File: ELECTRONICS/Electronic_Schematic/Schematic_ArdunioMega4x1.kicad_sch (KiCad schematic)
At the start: 66 parts, among them J1 AudioJack2

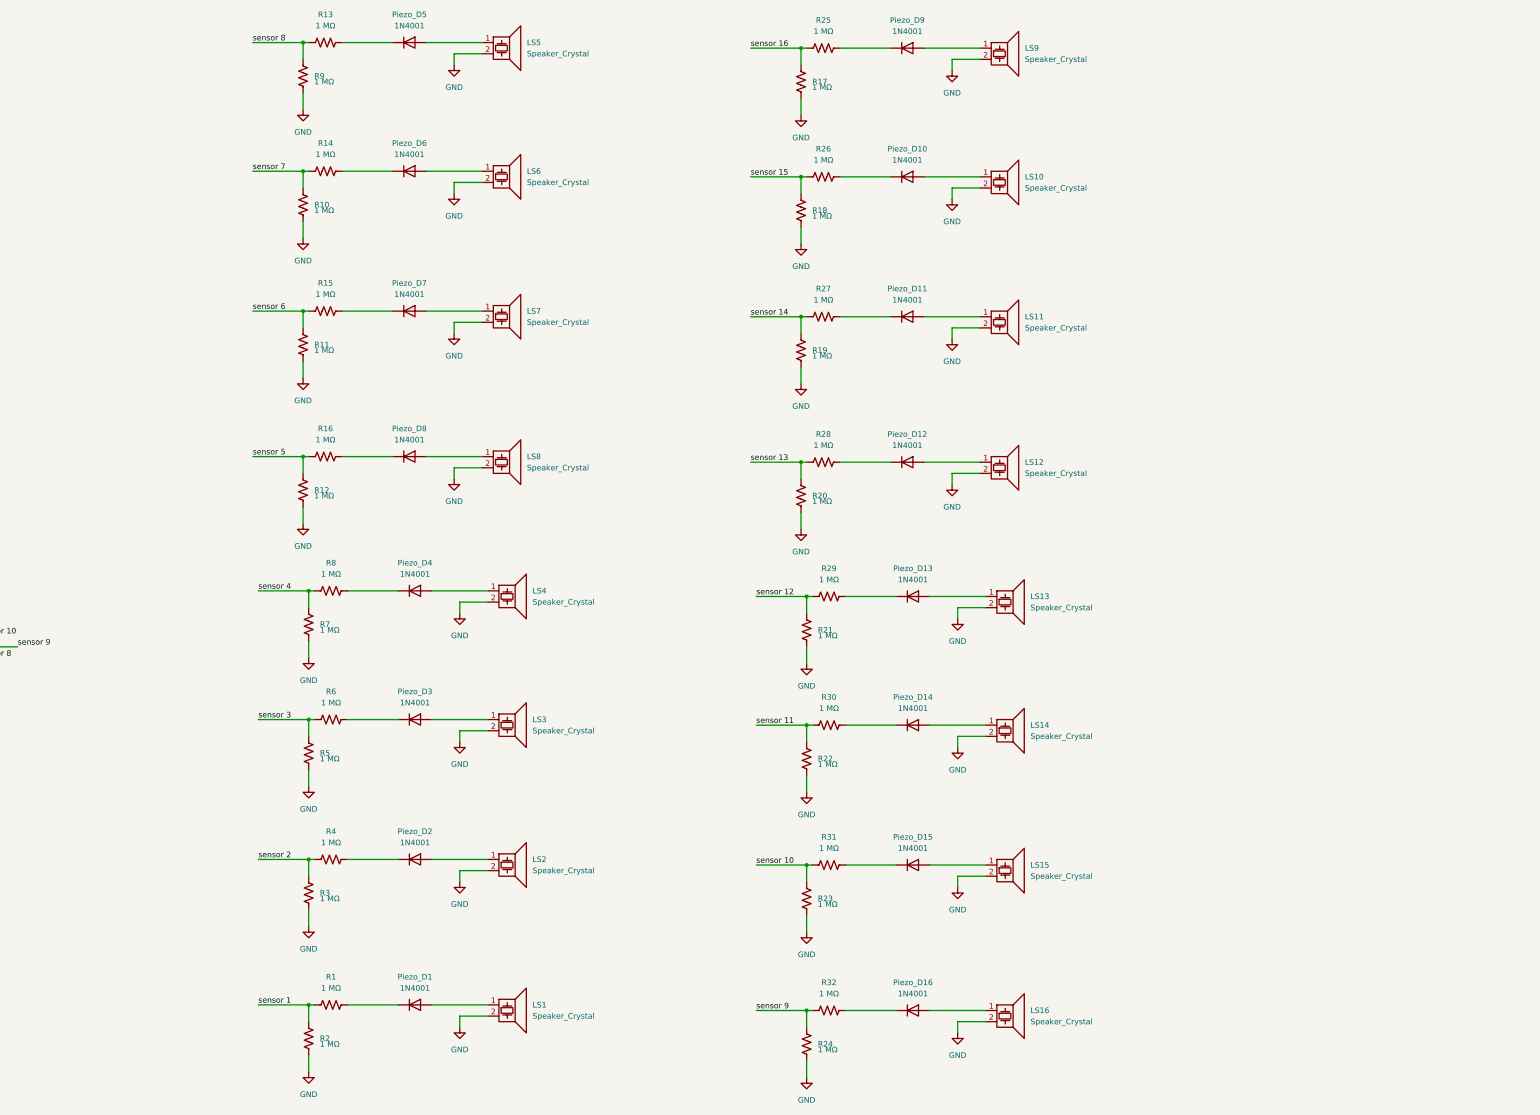
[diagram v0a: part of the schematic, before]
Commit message: added revision 3 of schematic
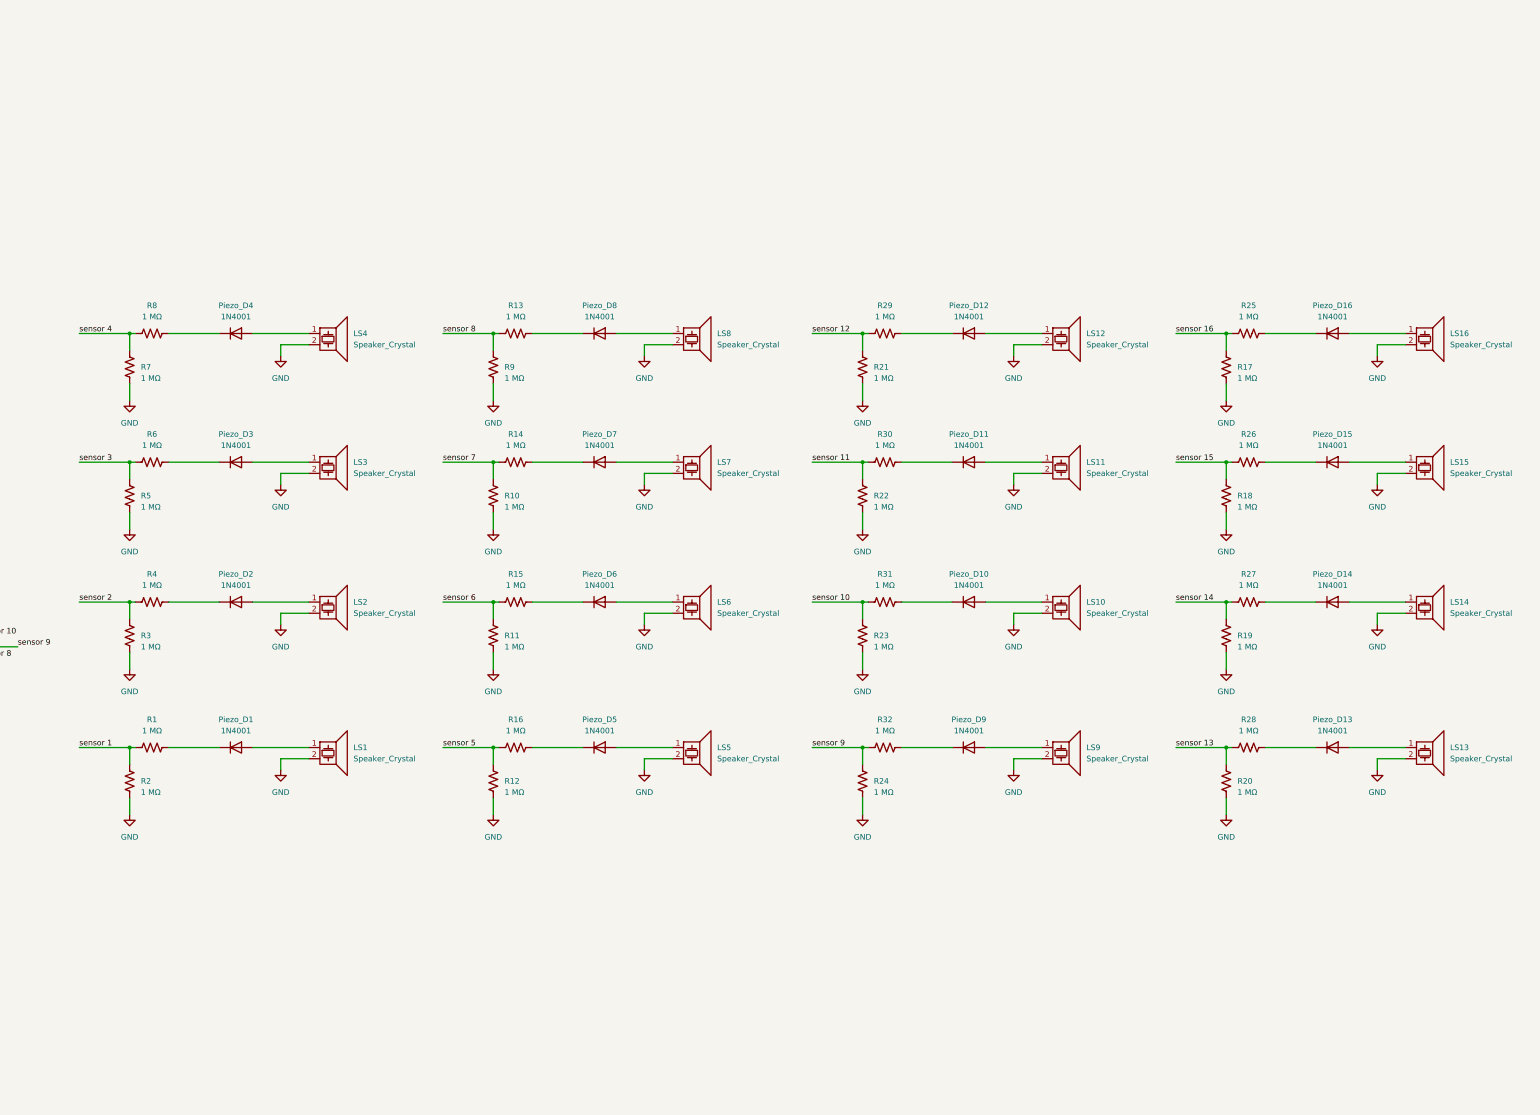
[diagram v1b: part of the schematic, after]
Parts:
- renumbered LS15 to LS10, LS14 to LS11, LS13 to LS12, LS12 to LS13, LS11 to LS14, LS10 to LS15, LS9 to LS16, LS8 to LS5, LS7 to LS6, LS6 to LS7, LS5 to LS8, LS16 to LS9, Piezo_D15 to Piezo_D10, Piezo_D14 to Piezo_D11, Piezo_D13 to Piezo_D12, Piezo_D12 to Piezo_D13, Piezo_D11 to Piezo_D14, Piezo_D10 to Piezo_D15, Piezo_D9 to Piezo_D16, Piezo_D8 to Piezo_D5, Piezo_D7 to Piezo_D6, Piezo_D6 to Piezo_D7, Piezo_D5 to Piezo_D8, Piezo_D16 to Piezo_D9
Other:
- moved on the sheet: LS1, LS10, LS11, LS12, LS13, LS14, LS15, LS16, LS2, LS3, LS4, LS5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
